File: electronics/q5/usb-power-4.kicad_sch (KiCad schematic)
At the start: 6 parts

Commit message: WIP: Q5 design-lock routing iteration snapshot (not verified)
Co-Authored-By: Claude Opus 5.5 <noreply@anthropic.com>
Claude-Session: https://claude.ai/code/session_01UrkzLMrBi6iLPSL5SbMCA7
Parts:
- removed R5: 10k, CountFidgetQ5:Resistor_SMD_R_0603_1608Metric, symbol CountFidgetQ5:R5
- removed R6: 100k, CountFidgetQ5:Resistor_SMD_R_0603_1608Metric, symbol CountFidgetQ5:R6
- added R30: 150k, CountFidgetQ5:Resistor_SMD_R_0603_1608Metric, symbol CountFidgetQ5:R30
- added R38: 100k, CountFidgetQ5:Resistor_SMD_R_0603_1608Metric, symbol CountFidgetQ5:R38
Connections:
- net SYS_ON: now also R38.2
- net VLOGIC_FB: now also R30.2
- new net VBUS_WAKE: R38.1
- new net VLOGIC: R30.1
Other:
- moved on the sheet: R31, R34, R35, R4

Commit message: Q5 design lock: JLC Basic substitutions, re-verified board, cost estimator
Co-Authored-By: Claude Opus 5.5 <noreply@anthropic.com>
Claude-Session: https://claude.ai/code/session_01UrkzLMrBi6iLPSL5SbMCA7
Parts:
- R34, R38: MPN RC0603FR-07100KL -> 0603WAF1003T5E
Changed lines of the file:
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@@
       (in_bom yes) (on_board yes) (dnp no)
  (property "Reference" "R34" (at 105.41 152.4 0) (effects (font (size 1.524 1.524)))) (property "Value" "100k" (at 105.41 156.21 0) (effects (font (size 1.524 1.524))))
-      (property "Footprint" "CountFidgetQ5:Resistor_SMD_R_0603_1608Metric" (at 105.41 161.29 0) (effects (font (size 1.27 1.27)) (hide yes))) (property "MPN" "RC0603FR-07100KL" (at 105.41 156.21 0) (effects (font (size 1.524 1.524)) (hide yes)))
+      (property "Footprint" "CountFidgetQ5:Resistor_SMD_R_0603_1608Metric" (at 105.41 161.29 0) (effects (font (size 1.27 1.27)) (hide yes))) (property "MPN" "0603WAF1003T5E" (at 105.41 156.21 0) (effects (font (size 1.524 1.524)) (hide yes)))
       (property "Description" "100k PWR_KEY pull-down; draws current only while COUNT is held." (at 105.41 161.29 0) (effects (font (size 1.27 1.27)) (hide yes)))
       (pin "1")(pin "2")
@@
       (in_bom yes) (on_board yes) (dnp no)
  (property "Reference" "R38" (at 105.41 229.87 0) (effects (font (size 1.524 1.524)))) (property "Value" "100k" (at 105.41 233.68 0) (effects (font (size 1.524 1.524))))
-      (property "Footprint" "CountFidgetQ5:Resistor_SMD_R_0603_1608Metric" (at 105.41 238.76 0) (effects (font (size 1.27 1.27)) (hide yes))) (property "MPN" "RC0603FR-07100KL" (at 105.41 233.68 0) (effects (font (size 1.524 1.524)) (hide yes)))
+      (property "Footprint" "CountFidgetQ5:Resistor_SMD_R_0603_1608Metric" (at 105.41 238.76 0) (effects (font (size 1.27 1.27)) (hide yes))) (property "MPN" "0603WAF1003T5E" (at 105.41 233.68 0) (effects (font (size 1.524 1.524)) (hide yes)))
       (property "Description" "100k series limit from D4 into U7 ON: with C40 filters VBUS hot-plug transients below the ON 6 V abs max." (at 105.41 238.76 0) (effects (font (size 1.27 1.27)) (hide yes)))
       (pin "1")(pin "2")

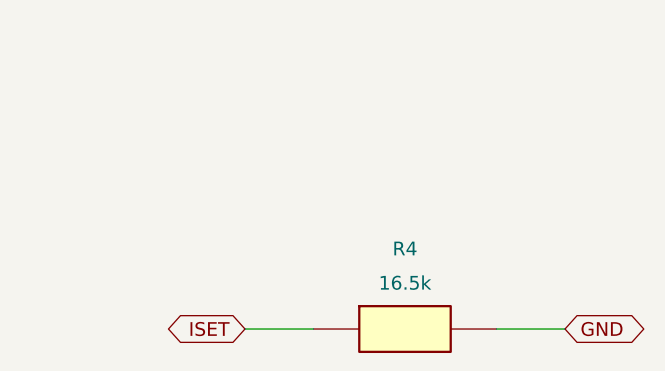
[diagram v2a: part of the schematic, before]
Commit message: Move nine part types to JLC Basic; 16 Extended types remain, each justified
R4 18k (16.7 mA charge), temperature window 56k/82k/18k/12k (7.26-35.83 C),
R32 75 ohm, Q1/Q2 AO3400A, 2.2 uF and 10 uF 50 V 0805 capacitors. Fresh
ERC/DRC/parity on unchanged routing, stock 42/42, exports, JLC footprint
fit and pin names, power/latch checks re-run. About $28 less per order.

Co-Authored-By: Claude Opus 5.5 <noreply@anthropic.com>
Claude-Session: https://claude.ai/code/session_01UrkzLMrBi6iLPSL5SbMCA7
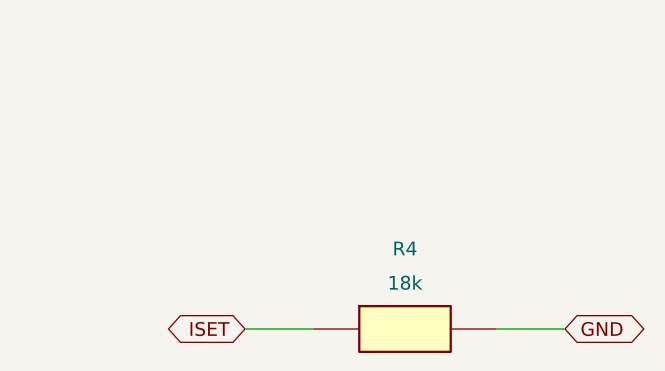
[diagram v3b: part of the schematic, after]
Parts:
- R4: value 16.5k -> 18k; MPN RC0603FR-0716K5L -> 0603WAF1802T5E
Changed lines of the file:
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@@
 (symbol (lib_id "CountFidgetQ5:R4") (at 294.64 238.76 0) (unit 1) (exclude_from_sim no)
       (in_bom yes) (on_board yes) (dnp no)
- (property "Reference" "R4" (at 294.64 229.87 0) (effects (font (size 1.524 1.524)))) (property "Value" "16.5k" (at 294.64 233.68 0) (effects (font (size 1.524 1.524))))
-      (property "Footprint" "CountFidgetQ5:Resistor_SMD_R_0603_1608Metric" (at 294.64 238.76 0) (effects (font (size 1.27 1.27)) (hide yes))) (property "MPN" "RC0603FR-0716K5L" (at 294.64 233.68 0) (effects (font (size 1.524 1.524)) (hide yes)))
+ (property "Reference" "R4" (at 294.64 229.87 0) (effects (font (size 1.524 1.524)))) (property "Value" "18k" (at 294.64 233.68 0) (effects (font (size 1.524 1.524))))
+      (property "Footprint" "CountFidgetQ5:Resistor_SMD_R_0603_1608Metric" (at 294.64 238.76 0) (effects (font (size 1.27 1.27)) (hide yes))) (property "MPN" "0603WAF1802T5E" (at 294.64 233.68 0) (effects (font (size 1.524 1.524)) (hide yes)))
       (property "Description" "1%, 0603, 0.1 W" (at 294.64 238.76 0) (effects (font (size 1.27 1.27)) (hide yes)))
       (pin "1")(pin "2")
